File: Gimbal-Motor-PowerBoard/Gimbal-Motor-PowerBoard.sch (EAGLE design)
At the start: 45 parts, among them Q1 MOSFET-NCHANNELFQP30N06L, Q2 MOSFET-NCHANNELFQP30N06L, Q3 MOSFET-NCHANNELFQP30N06L, Q4 MOSFET-NCHANNELFQP30N06L, U1 NUP4201MR6

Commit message: Finished adding comps and changing labels
All components that will be on gimbal pwer board have been added and wires have been renamed to match gimbal design. Last schematic change to make is label header pins.
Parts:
- added C25: 2.2u, SparkFun-Passives:CAP1206
- added C26: 0.1u, SparkFun-Passives:CAP0805
- added D14, D15, D16: 15V, SparkFun-DiscreteSemi:DIODE-ZENER3.3V
- added D6: (no value), SparkFun-LED:LED1206
- added J3: APP_2POS_CONFIG5V_HORIZ, MRDT-Connectors:APP_2POS_CONFIG5V_HORIZ
- added Q5, Q6: MOSFET-NCHANNELFQP30N06L, SparkFun-DiscreteSemi:MOSFET-NCHANNELFQP30N06L
- added Q9: MOSFET-NCHANNELAO3404A, SparkFun-DiscreteSemi:MOSFET-NCHANNELAO3404A
- added R21, R22: 10, SparkFun-Passives:RESISTOR0805-RES
- added R24: 46.4k, SparkFun-Passives:RESISTOR0805-RES
- added R25: 4.99k, SparkFun-Passives:RESISTOR0805-RES
- added R32: 330, SparkFun-Passives:RESISTOR0805-RES
- added R50: 3M, SparkFun-Passives:RESISTOR0805-RES
- added R51: 1M, SparkFun-Passives:RESISTOR0805-RES
- added SH1, SH2: SHORT-HT5, BLDC_Motor_Controller_2016_Rev1:SHORT-HT5
- added SV1, SV2: (no value), con-lstb:MA13-1
- added U$18, U$19, U$20, U$26, U$27, U$28, U$29: TEST_POINT_0.1INDIAM, MRDT-Connectors:TEST_POINT_0.1INDIAM
- added U$5, U$6, U$7: APPPP45_PCB_HORIZ_RIGHT, MRDT-Connectors:APPPP45_PCB_HORIZ_RIGHT
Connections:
- removed net 12V: C1.+, C10.1, C2.+, C3.+, C4.+, C5.+, C6.+, C7.+, C8.+, C9.1, R2.2
- new net 12V_ACT: C1.+, C10.1, C19.1, C2.+, C22.1, C25.1, C3.+, C4.+, C5.+, C6.+, C7.+, C8.+, C9.1, J3VCC.P$1, Q1.D, Q3.D, Q5.D, R2.2, SV1.12
- new net GH_C: R21.2
- new net GL_C: R22.2
- new net N$10: SV1.13
- new net N$11: SV2.13
- new net N$12: SV2.12
- new net N$17: D14.C, Q5.G, R21.1, U$18.P$1
- new net N$18: D15.C, Q6.G, R22.1, U$19.P$1
- new net N$19: SV2.11
- new net N$2: SV1.11
- new net N$20: SV2.10
- new net N$21: SV2.9
- new net N$22: SV2.8
- new net N$23: D6.C, R32.1
- new net N$24: SV2.7
- new net N$25: SV2.6
- new net N$26: SV2.5
- new net N$27: SV2.4
- new net N$28: SV2.3
- new net N$29: SV2.2
- new net N$30: SV2.1
- new net N$38: D16.C, Q9.G, R50.2, R51.1
- new net N$4: SV1.7
- new net N$41: D16.A, D6.A, Q9.S
- new net N$5: SV1.5
- new net N$6: SV1.3
- new net N$7: SV1.1
- new net N$8: SV1.4
- new net N$9: SV1.2
- new net SH_C: D14.A, Q5.S, Q6.D, R24.1, U$20.P$1, U$7.P$1
- new net SP1: SH2.P$1
- new net SP2: SH1.P$1
- net ASENSE: now also SV1.10
- net BSENSE: now also SV1.8
- net CSENSE: now also C26.1, R24.2, R25.1, SV1.6
- net GND: now also C11.2, C25.2, C26.2, D15.A, J3GND.P$1, Q6.S, R25.2, R3.1, R32.2, R51.2, SH1.P$2, SH2.P$2, U$26.P$1, U$27.P$1, U$28.P$1, U$29.P$1
- net N$3: now also SV1.9; no longer C11.2, R3.1
- net PVDD: now also R50.1; no longer C19.1, C22.1, Q1.D, Q3.D
- net SH_A: now also U$5.P$1
- net SH_B: now also U$6.P$1
- net VCC: now also Q9.D
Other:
- note added: "External Connections"
- note added: "Header to Control Card"
- note added: "Phase C"
- note added: "Power Indication"
- moved on the sheet: C19, C20, C21, C22, C23, C24, D10, D11, D12, D13, Q1, Q2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

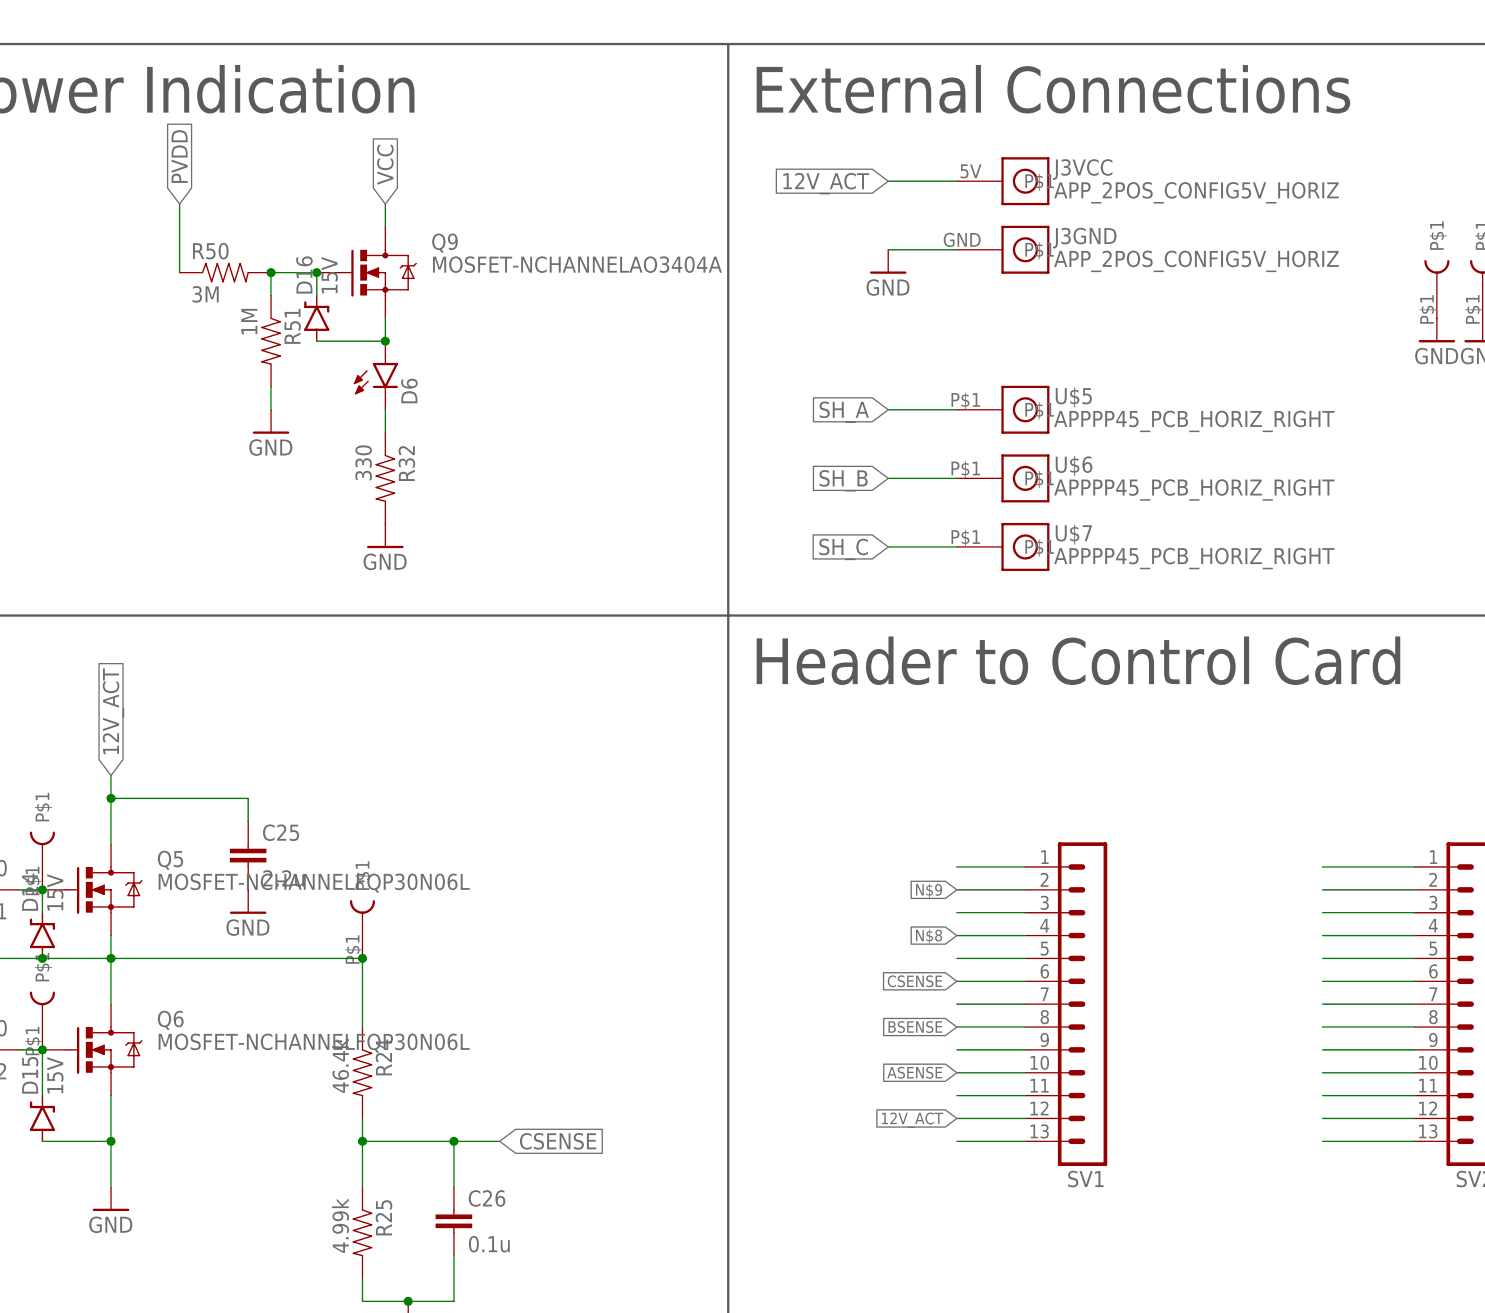
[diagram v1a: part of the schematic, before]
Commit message: Header pins to control card named
All traces that will go to control card have been named on a header pin and can be rearanged for more convienent layout. Power indication simplified.
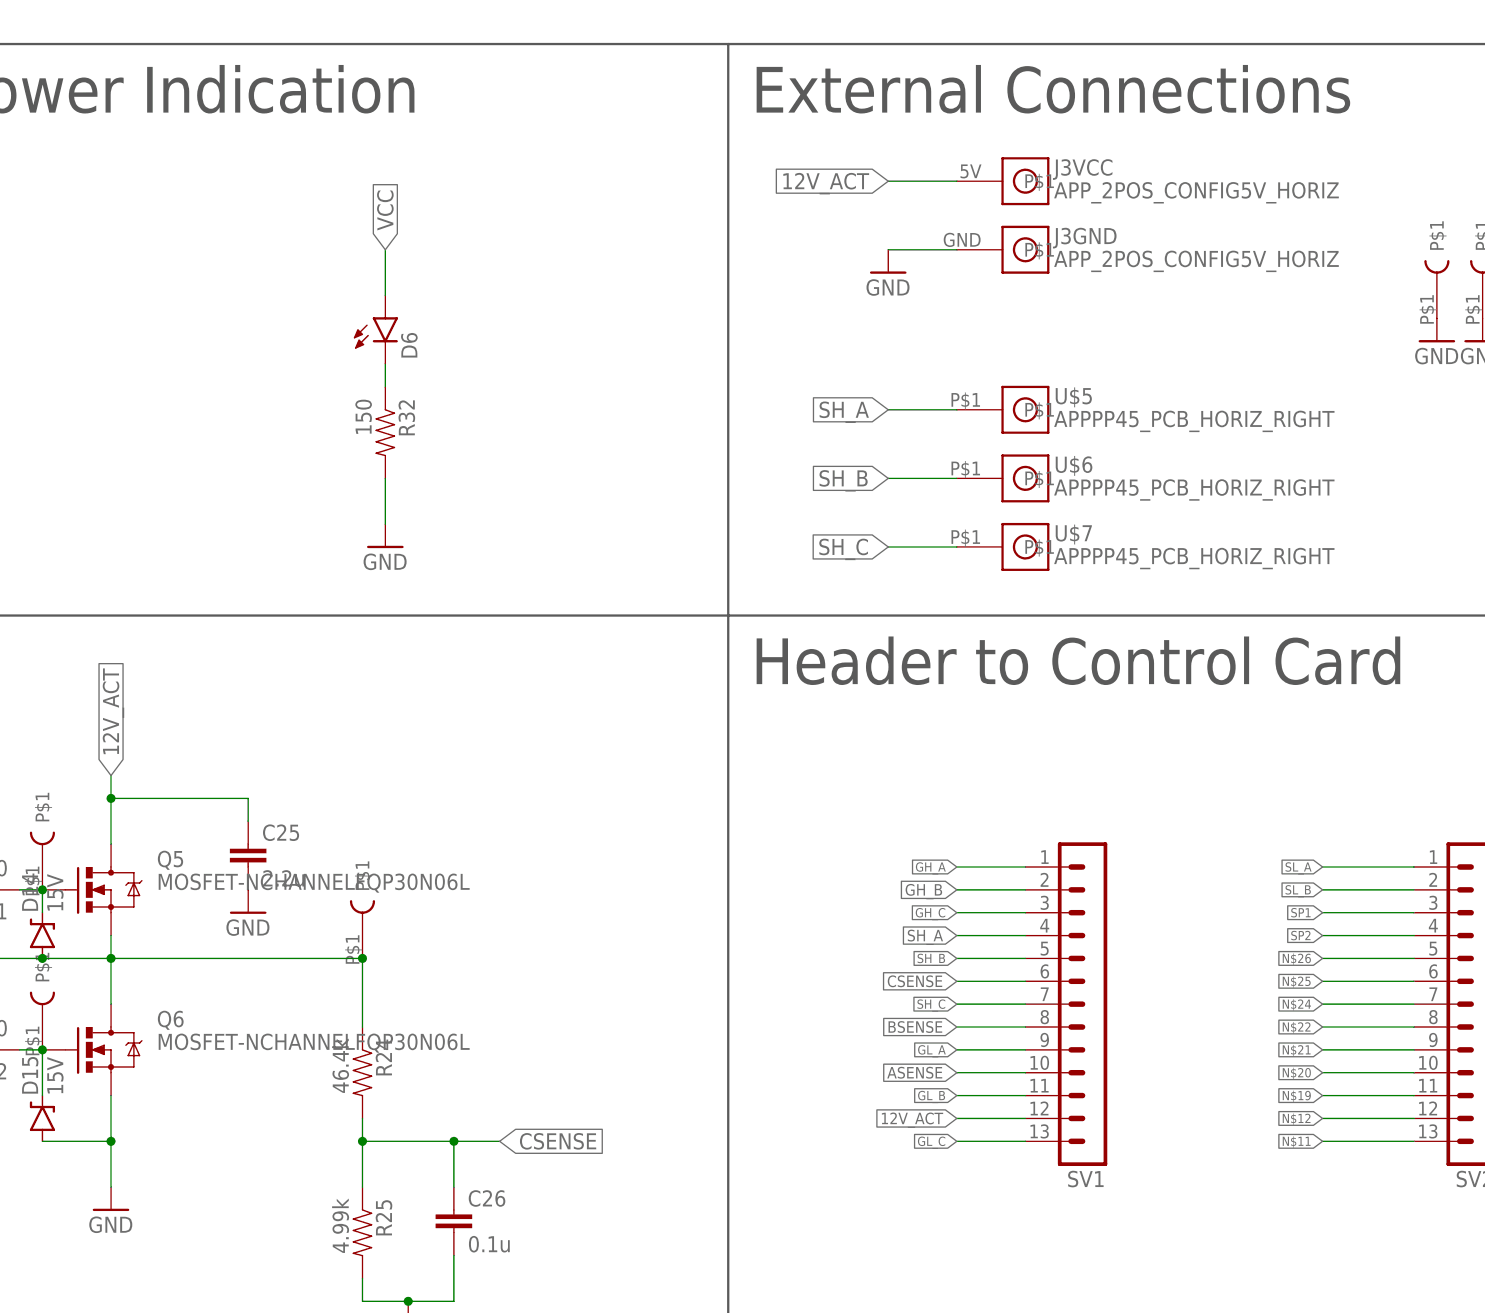
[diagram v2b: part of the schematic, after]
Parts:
- removed D16: 15V, SparkFun-DiscreteSemi:DIODE-ZENER3.3V
- removed Q9: MOSFET-NCHANNELAO3404A, SparkFun-DiscreteSemi:MOSFET-NCHANNELAO3404A
- removed R50: 3M, SparkFun-Passives:RESISTOR0805-RES
- removed R51: 1M, SparkFun-Passives:RESISTOR0805-RES
- R32: value 330 -> 150
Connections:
- removed net N$10: SV1.13
- removed net N$2: SV1.11
- removed net N$27: SV2.4
- removed net N$28: SV2.3
- removed net N$29: SV2.2
- removed net N$3: SV1.9
- removed net N$30: SV2.1
- removed net N$38: D16.C, Q9.G, R50.2, R51.1
- removed net N$4: SV1.7
- removed net N$41: D16.A, D6.A, Q9.S
- removed net N$5: SV1.5
- removed net N$6: SV1.3
- removed net N$7: SV1.1
- removed net N$8: SV1.4
- removed net N$9: SV1.2
- removed net PVDD: R50.1
- net GH_A: now also SV1.1
- net GH_B: now also SV1.2
- net GH_C: now also SV1.3
- net GL_A: now also SV1.9
- net GL_B: now also SV1.11
- net GL_C: now also SV1.13
- net GND: no longer R51.2
- net SH_A: now also SV1.4
- net SH_B: now also SV1.5
- net SH_C: now also SV1.7
- net SL_A: now also SV2.1
- net SL_B: now also SV2.2
- net SP1: now also SV2.3
- net SP2: now also SV2.4
- net VCC: now also D6.A; no longer Q9.D
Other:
- moved on the sheet: D6, R32
